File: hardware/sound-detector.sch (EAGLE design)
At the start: 38 parts, among them IC1 LMV324

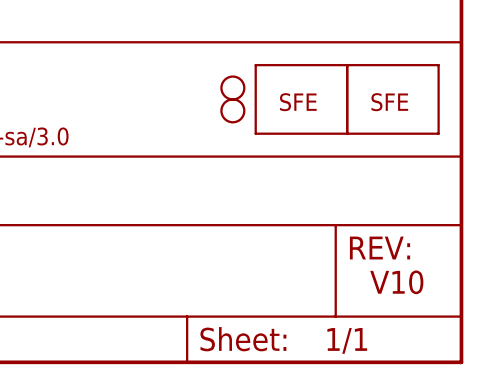
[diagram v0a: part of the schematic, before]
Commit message: Fixing incorrect version number on schematic
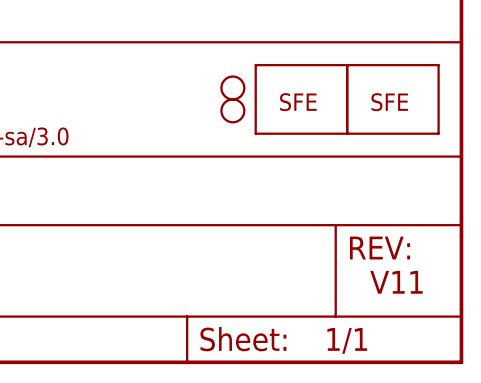
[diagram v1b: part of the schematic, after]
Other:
- note added: "V11"
- note removed: "V10"
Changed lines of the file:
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@@
 <?xml version="1.0" encoding="utf-8"?>
 <!DOCTYPE eagle SYSTEM "eagle.dtd">
-<eagle version="6.5.0">
+<eagle version="7.7.0">
 <drawing>
 <settings>
@@
 <layer number="254" name="cooling" color="7" fill="1" visible="no" active="yes"/>
 </layers>
-<schematic xreflabel="%F%N/%S.%C%R" xrefpart="/%S.%C%R">
+<schematic xreflabel="%F%N/%S" xrefpart="/%S">
 <attributes>
 </attributes>
@@
 <plain>
 <text x="167.64" y="10.16" size="2.54" layer="94" font="vector">Byron Jacquot</text>
-<text x="238.76" y="7.62" size="2.54" layer="94">V10</text>
+<text x="238.76" y="7.62" size="2.54" layer="94">V11</text>
 <text x="66.04" y="60.96" size="1.778" layer="97" font="vector">Supply decoupling - place near U1</text>
 <wire x1="0" y1="104.14" x2="60.96" y2="104.14" width="0.2032" layer="97" style="longdash"/>
